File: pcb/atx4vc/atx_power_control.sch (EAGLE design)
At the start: 61 parts, among them IC2 REG1117, IC3 STM32F042F4, IC4 MY_7905DT, J1 ATX24RH, SW1 324_SW, SW2 324_SW, SW3 324_SW, SW4 324_SW, SW5 324_SW, SW6 324_SW, SW7 324_SW, U1 USBC_16P, U2 USBC_16P

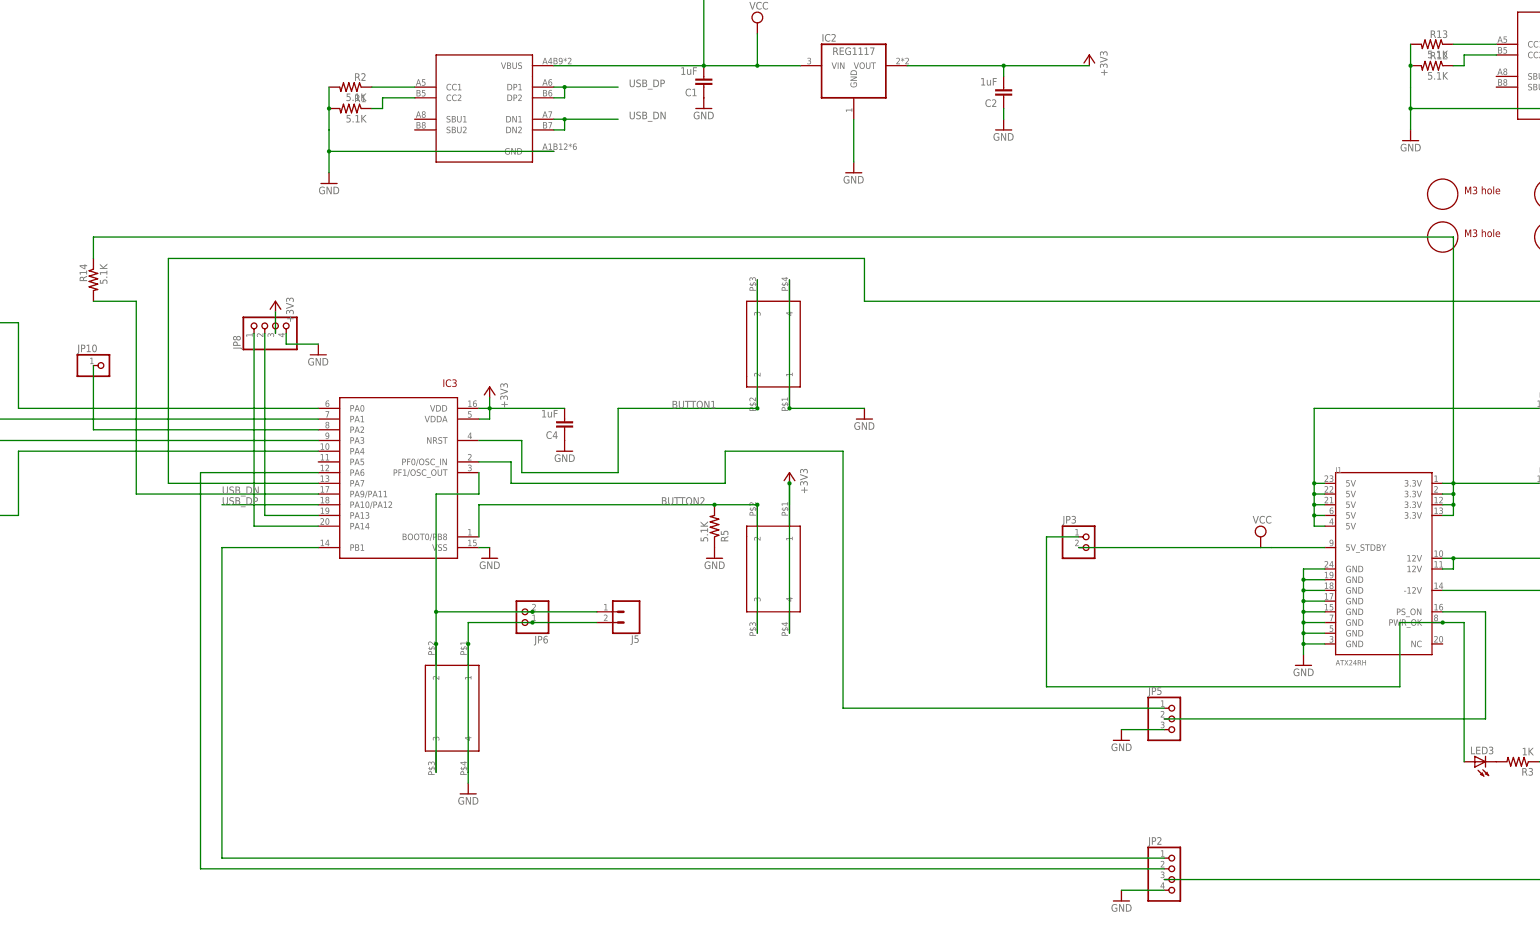
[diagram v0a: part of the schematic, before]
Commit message: fixed led board silkscreen, changed ATX4VC to use PG signal
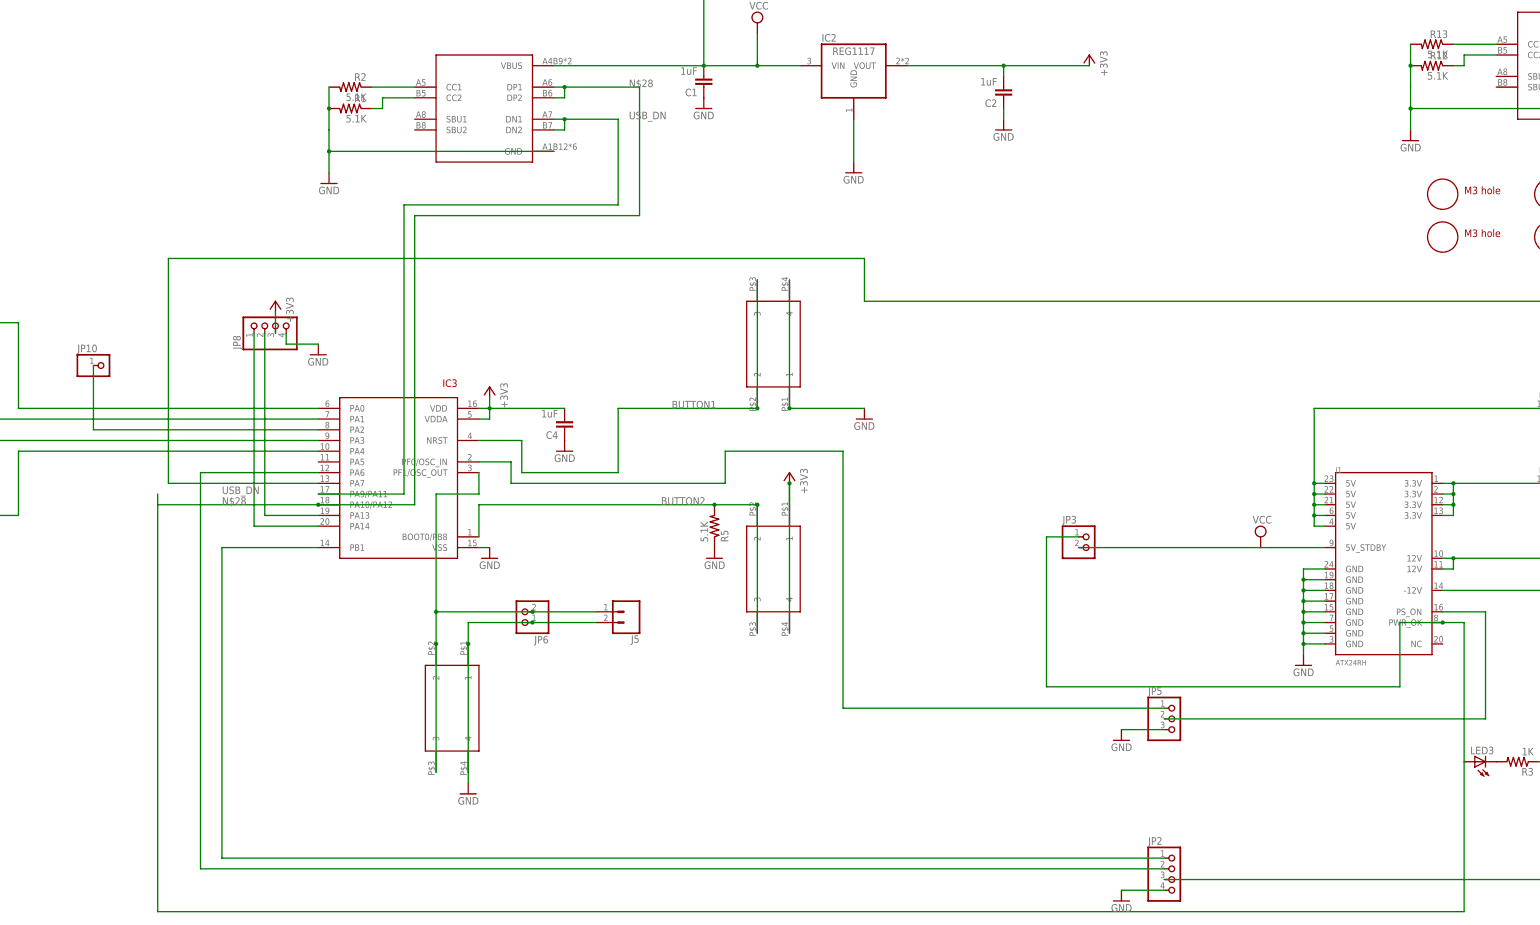
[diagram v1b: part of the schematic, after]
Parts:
- removed R14: 5.1K, joyAnalog:RESISTOR0805-RES
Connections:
- removed net N$12: F3.1, J1.3.3V@0, J1.3.3V@1, J1.3.3V@2, J1.3.3V@3, R14.1
- removed net USB_DP: IC3.PA10/PA12, U2.DP1, U2.DP2
- new net N$14: F3.1, J1.3.3V@0, J1.3.3V@1, J1.3.3V@2, J1.3.3V@3
- net N$28: now also IC3.PA10/PA12, U2.DP1, U2.DP2
- net USB_DN: no longer R14.2
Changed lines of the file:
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@@
 <part name="R12" library="joyAnalog" deviceset="RESISTOR" device="0805-RES" value="5.1K"/>
 <part name="R13" library="joyAnalog" deviceset="RESISTOR" device="0805-RES" value="5.1K"/>
-<part name="R14" library="joyAnalog" deviceset="RESISTOR" device="0805-RES" value="5.1K"/>
 </parts>
 <sheets>
@@
 <attribute name="NAME" x="250.19" y="128.4986" size="1.778" layer="95" rot="MR0"/>
 <attribute name="VALUE" x="250.19" y="123.698" size="1.778" layer="96" rot="MR0"/>
-</instance>
-<instance part="R14" gate="G$1" x="-71.12" y="71.12" smashed="yes" rot="MR270">
-<attribute name="NAME" x="-72.6186" y="74.93" size="1.778" layer="95" rot="MR270"/>
-<attribute name="VALUE" x="-67.818" y="74.93" size="1.778" layer="96" rot="MR270"/>
-<attribute name="NAME" x="-72.6186" y="74.93" size="1.778" layer="95" rot="MR270"/>
-<attribute name="VALUE" x="-67.818" y="74.93" size="1.778" layer="96" rot="MR270"/>
 </instance>
 </instances>
@@
 </segment>
 </net>
-<net name="USB_DP" class="0">
-<segment>
-<wire x1="53.34" y1="116.84" x2="40.64" y2="116.84" width="0.1524" layer="91"/>
-<label x="55.88" y="116.84" size="1.778" layer="95"/>
-<pinref part="U2" gate="G$1" pin="DP1"/>
-<wire x1="40.64" y1="116.84" x2="38.1" y2="116.84" width="0.1524" layer="91"/>
-<wire x1="40.64" y1="116.84" x2="40.64" y2="114.3" width="0.1524" layer="91"/>
-<junction x="40.64" y="116.84"/>
-<pinref part="U2" gate="G$1" pin="DP2"/>
-<wire x1="40.64" y1="114.3" x2="38.1" y2="114.3" width="0.1524" layer="91"/>
-</segment>
-<segment>
-<pinref part="IC3" gate="G$1" pin="PA10/PA12"/>
-<wire x1="-17.78" y1="17.78" x2="-40.64" y2="17.78" width="0.1524" layer="91"/>
-<label x="-40.64" y="17.78" size="1.778" layer="95"/>
-</segment>
-</net>
 <net name="N$31" class="0">
 <segment>
@@
 <net name="USB_DN" class="0">
 <segment>
+<pinref part="IC3" gate="G$1" pin="PA9/PA11"/>
+<label x="-40.64" y="20.32" size="1.778" layer="95"/>
+<wire x1="-17.78" y1="20.32" x2="2.54" y2="20.32" width="0.1524" layer="91"/>
+<wire x1="2.54" y1="20.32" x2="2.54" y2="88.9" width="0.1524" layer="91"/>
 <wire x1="53.34" y1="109.22" x2="40.64" y2="109.22" width="0.1524" layer="91"/>
 <pinref part="U2" gate="G$1" pin="DN1"/>
@@
 <wire x1="40.64" y1="106.68" x2="40.64" y2="109.22" width="0.1524" layer="91"/>
 <junction x="40.64" y="109.22"/>
-</segment>
-<segment>
-<pinref part="IC3" gate="G$1" pin="PA9/PA11"/>
-<wire x1="-60.96" y1="20.32" x2="-17.78" y2="20.32" width="0.1524" layer="91"/>
-<label x="-40.64" y="20.32" size="1.778" layer="95"/>
-<wire x1="-60.96" y1="20.32" x2="-60.96" y2="66.04" width="0.1524" layer="91"/>
-<pinref part="R14" gate="G$1" pin="2"/>
-<wire x1="-60.96" y1="66.04" x2="-71.12" y2="66.04" width="0.1524" layer="91"/>
+<wire x1="2.54" y1="88.9" x2="53.34" y2="88.9" width="0.1524" layer="91"/>
+<wire x1="53.34" y1="88.9" x2="53.34" y2="109.22" width="0.1524" layer="91"/>
 </segment>
 </net>
@@
 <wire x1="365.76" y1="-17.78" x2="365.76" y2="-15.24" width="0.1524" layer="91"/>
 <junction x="347.98" y="-17.78"/>
-</segment>
-</net>
-<net name="N$12" class="0">
-<segment>
-<pinref part="J1" gate="G$1" pin="3.3V@0"/>
-<wire x1="248.92" y1="22.86" x2="251.46" y2="22.86" width="0.1524" layer="91"/>
-<wire x1="251.46" y1="22.86" x2="251.46" y2="20.32" width="0.1524" layer="91"/>
-<pinref part="J1" gate="G$1" pin="3.3V@3"/>
-<wire x1="251.46" y1="20.32" x2="251.46" y2="17.78" width="0.1524" layer="91"/>
-<wire x1="251.46" y1="17.78" x2="251.46" y2="15.24" width="0.1524" layer="91"/>
-<wire x1="251.46" y1="15.24" x2="248.92" y2="15.24" width="0.1524" layer="91"/>
-<pinref part="J1" gate="G$1" pin="3.3V@2"/>
-<wire x1="248.92" y1="17.78" x2="251.46" y2="17.78" width="0.1524" layer="91"/>
-<junction x="251.46" y="17.78"/>
-<pinref part="J1" gate="G$1" pin="3.3V@1"/>
-<wire x1="248.92" y1="20.32" x2="251.46" y2="20.32" width="0.1524" layer="91"/>
-<junction x="251.46" y="20.32"/>
-<wire x1="251.46" y1="22.86" x2="271.78" y2="22.86" width="0.1524" layer="91"/>
-<junction x="251.46" y="22.86"/>
-<pinref part="F3" gate="G$1" pin="1"/>
-<wire x1="251.46" y1="22.86" x2="251.46" y2="81.28" width="0.1524" layer="91"/>
-<wire x1="251.46" y1="81.28" x2="-71.12" y2="81.28" width="0.1524" layer="91"/>
-<pinref part="R14" gate="G$1" pin="1"/>
-<wire x1="-71.12" y1="81.28" x2="-71.12" y2="76.2" width="0.1524" layer="91"/>
 </segment>
 </net>
@@
 <pinref part="JP3" gate="G$1" pin="1"/>
 <wire x1="154.94" y1="10.16" x2="162.56" y2="10.16" width="0.1524" layer="91"/>
+<pinref part="IC3" gate="G$1" pin="PA10/PA12"/>
+<wire x1="-17.78" y1="17.78" x2="-55.88" y2="17.78" width="0.1524" layer="91"/>
+<label x="-40.64" y="17.78" size="1.778" layer="95"/>
+<wire x1="-17.78" y1="17.78" x2="5.08" y2="17.78" width="0.1524" layer="91"/>
+<wire x1="5.08" y1="17.78" x2="5.08" y2="86.36" width="0.1524" layer="91"/>
+<junction x="-17.78" y="17.78"/>
+<wire x1="5.08" y1="86.36" x2="58.42" y2="86.36" width="0.1524" layer="91"/>
+<wire x1="58.42" y1="116.84" x2="40.64" y2="116.84" width="0.1524" layer="91"/>
+<label x="55.88" y="116.84" size="1.778" layer="95"/>
+<pinref part="U2" gate="G$1" pin="DP1"/>
+<wire x1="40.64" y1="116.84" x2="38.1" y2="116.84" width="0.1524" layer="91"/>
+<wire x1="40.64" y1="116.84" x2="40.64" y2="114.3" width="0.1524" layer="91"/>
+<junction x="40.64" y="116.84"/>
+<pinref part="U2" gate="G$1" pin="DP2"/>
+<wire x1="40.64" y1="114.3" x2="38.1" y2="114.3" width="0.1524" layer="91"/>
+<wire x1="58.42" y1="86.36" x2="58.42" y2="116.84" width="0.1524" layer="91"/>
+<wire x1="254" y1="-43.18" x2="254" y2="-78.74" width="0.1524" layer="91"/>
+<wire x1="254" y1="-78.74" x2="-55.88" y2="-78.74" width="0.1524" layer="91"/>
+<wire x1="-55.88" y1="-78.74" x2="-55.88" y2="17.78" width="0.1524" layer="91"/>
+<wire x1="-55.88" y1="20.32" x2="-55.88" y2="17.78" width="0.1524" layer="91"/>
 </segment>
 </net>
@@
 </segment>
 </net>
+<net name="N$14" class="0">
+<segment>
+<pinref part="J1" gate="G$1" pin="3.3V@3"/>
+<pinref part="F3" gate="G$1" pin="1"/>
+<pinref part="J1" gate="G$1" pin="3.3V@0"/>
+<wire x1="248.92" y1="22.86" x2="251.46" y2="22.86" width="0.1524" layer="91"/>
+<wire x1="251.46" y1="22.86" x2="271.78" y2="22.86" width="0.1524" layer="91"/>
+<junction x="251.46" y="22.86"/>
+<wire x1="251.46" y1="22.86" x2="251.46" y2="20.32" width="0.1524" layer="91"/>
+<pinref part="J1" gate="G$1" pin="3.3V@1"/>
+<wire x1="248.92" y1="20.32" x2="251.46" y2="20.32" width="0.1524" layer="91"/>
+<junction x="251.46" y="20.32"/>
+<wire x1="251.46" y1="20.32" x2="251.46" y2="17.78" width="0.1524" layer="91"/>
+<pinref part="J1" gate="G$1" pin="3.3V@2"/>
+<wire x1="248.92" y1="17.78" x2="251.46" y2="17.78" width="0.1524" layer="91"/>
+<junction x="251.46" y="17.78"/>
+<wire x1="251.46" y1="17.78" x2="251.46" y2="15.24" width="0.1524" layer="91"/>
+<wire x1="251.46" y1="15.24" x2="248.92" y2="15.24" width="0.1524" layer="91"/>
+</segment>
+</net>
